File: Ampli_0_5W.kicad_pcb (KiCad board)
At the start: 2 copper layers, 100 x 81 mm, 70 parts, among them J1002 RF_In, J1003 PTT_In, J1005 Aux_PTT_Out, J1006 RF_Out, Q1001 2N7002, Q1002 FDD6685, Q1005 2N5109, Q1006 AFT05MP075N, T1001 4:1, T1002 1:1, T1003 1:9, U1001 L78L05_SO8

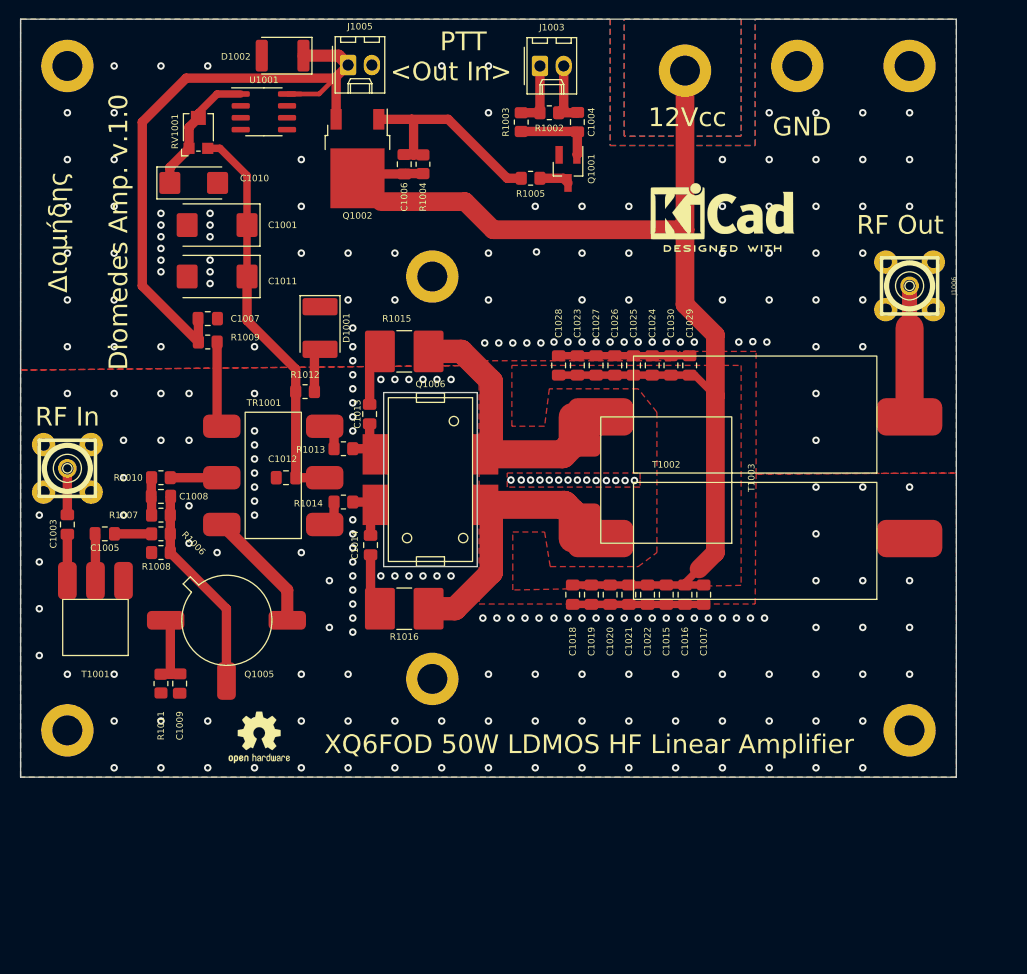
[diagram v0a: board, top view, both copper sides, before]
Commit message: release 2.0, shorter drain path
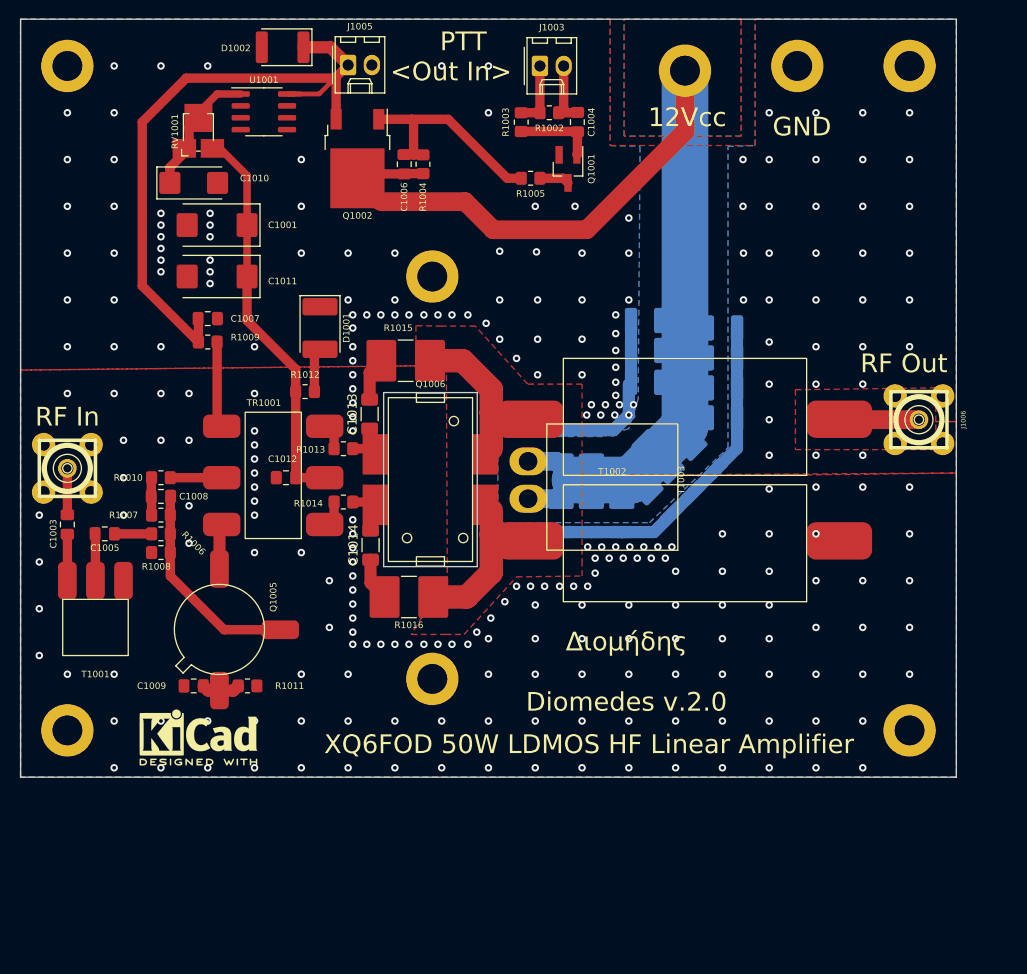
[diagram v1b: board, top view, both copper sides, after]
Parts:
- removed the REF** at (155.0, 50.5)
- removed the REF** at (105.5, 106.8)
- added REF**: KiCad-Logo2_5mm_SilkScreen, Symbol:KiCad-Logo2_5mm_SilkScreen, F.Cu at (99.0, 106.8)
- C1013, C1014: footprint Capacitor_SMD:C_0805_2012Metric_Pad1.18x1.45mm_HandSolder -> Capacitor_SMD:C_1206_3216Metric_Pad1.33x1.80mm_HandSolder
- C1015, C1016, C1017, C1018, C1019, C1020, C1021, C1022, C1023, C1024, C1025, C1026, C1027, C1028, C1029, C1030: footprint Capacitor_SMD:C_0805_2012Metric_Pad1.18x1.45mm_HandSolder -> Capacitor_SMD:C_1210_3225Metric_Pad1.33x2.70mm_HandSolder; moved to B.Cu
- moved C1017 22.2 mm to (155.0, 69.4), turned to 180 degrees
- moved C1016 19.3 mm to (155.0, 72.6), turned to 180 degrees
- moved C1015 15.1 mm to (153.2, 77.0), turned to 135 degrees
- moved J1006 14.3 mm to (176.0, 72.8)
- moved C1029 13.5 mm to (141.0, 75.5)
- moved C1022 12.6 mm to (150.8, 79.5), turned to 135 degrees
- moved C1021 10.4 mm to (148.5, 81.8), turned to 135 degrees
- moved R1011 9.25 mm to (104.2, 101.2), turned to 180 degrees
- moved C1023 9.22 mm to (145.5, 74.0), turned to -45 degrees
- moved C1028 8.50 mm to (137.8, 75.5)
- moved C1024 8.50 mm to (155.0, 63.0), turned to 180 degrees
- moved C1018 8.34 mm to (137.8, 83.2)
- moved C1020 8.34 mm to (144.2, 83.2)
- moved C1019 8.25 mm to (141.0, 83.2)
- moved T1003 7.50 mm to (151.5, 79.2)
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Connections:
- T1002 pad 1: Net-(Q1006-Pad3) -> decoupling
- T1002 pad 3: Net-(Q1006-Pad4) -> decoupling
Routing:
- net GND: track 35.2 -> 59.9 mm, vias 243 -> 269
- net decoupling: track 136.4 -> 122.3 mm
- net Net-(Q1006-Pad4): track 27.8 -> 18.7 mm
- net Net-(Q1006-Pad3): track 27.2 -> 18.4 mm
- net Net-(Q1005-Pad3): track 13.1 -> 4.85 mm
- net Net-(J1006-Pad1): track 14.0 -> 8.52 mm
- net Net-(C1009-Pad2): track 7.99 -> 4.13 mm
- net Net-(C1014-Pad2): track 5.99 -> 3.23 mm
- net Net-(C1013-Pad1): track 5.31 -> 2.65 mm
- net Net-(C1014-Pad1): track 6.18 -> 4.61 mm
- net Net-(C1013-Pad2): track 6.12 -> 4.66 mm
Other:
- board text added: "Διομήδης Diomedes v.2.0"
- board text removed: "Διομήδης Diomedes Amp. v.1.0"

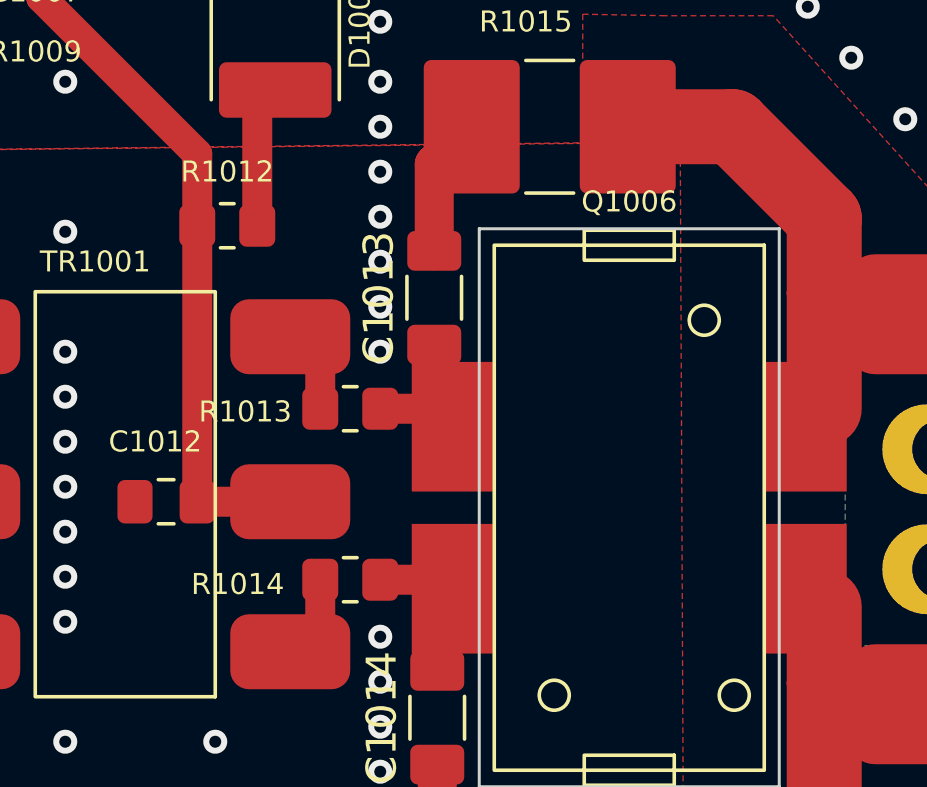
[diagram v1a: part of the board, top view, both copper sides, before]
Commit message: shorten drain circuit, new gerber, new ibom
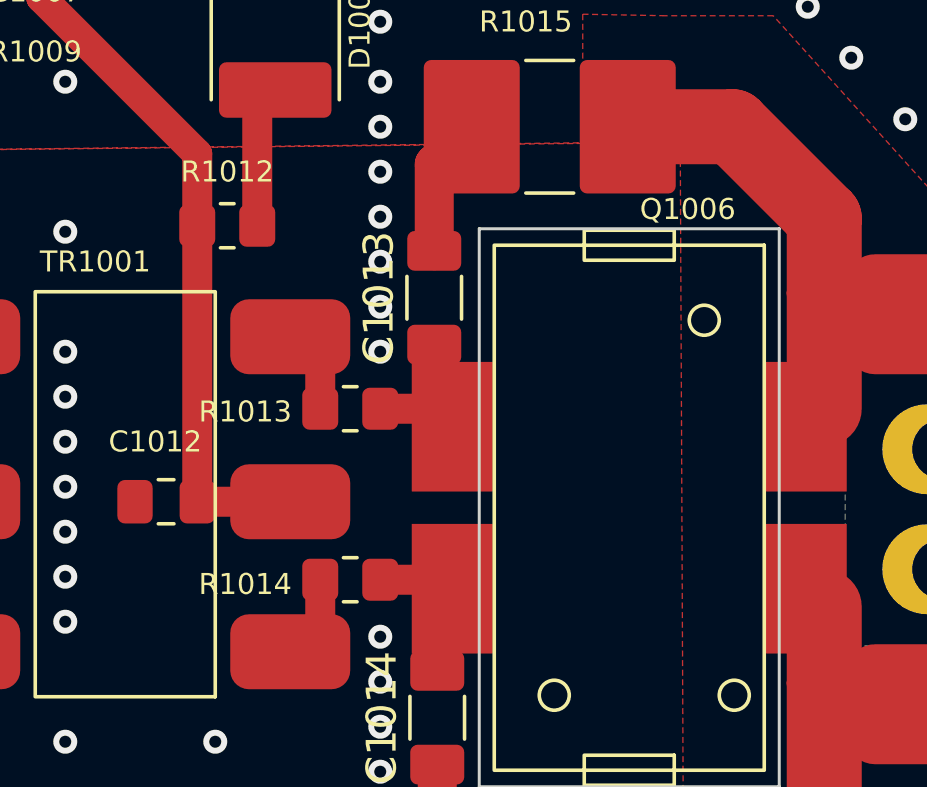
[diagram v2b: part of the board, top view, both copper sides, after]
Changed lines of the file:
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@@
     (property "Sheetname" "")
     (attr smd)
-    (fp_text reference "Q1006" (at 0 10.95 unlocked) (layer "F.SilkS")
+    (fp_text reference "Q1006" (at -1.95 10.7 unlocked) (layer "F.SilkS")
       (effects (font (size 0.7 0.7) (thickness 0.175)))
     )
@@
     (property "Sheetname" "")
     (attr smd)
-    (fp_text reference "R1014" (at 3.75 -0.15) (layer "F.SilkS")
+    (fp_text reference "R1014" (at 3.5 -0.15) (layer "F.SilkS")
       (effects (font (size 0.7 0.7) (thickness 0.15)))
     )
@@
     (effects (font (size 2 2) (thickness 0.4)))
   )
+  (dimension (type aligned) (layer "F.SilkS")
+    (pts (xy 131 80.25) (xy 90.5 80.5))
+    (height -61.983387)
+    (gr_text "40.5008 mm" (at 111.125507 141.207228 0.3536731592) (layer "F.SilkS")
+      (effects (font (size 1 1) (thickness 0.15)))
+    )
+    (format (units 3) (units_format 1) (precision 4))
+    (style (thickness 0.15) (arrow_length 1.27) (text_position_mode 0) (extension_height 0.58642) (extension_offset 0.5) keep_text_aligned)
+  )
+  (dimension (type aligned) (layer "F.SilkS")
+    (pts (xy 109.75 111) (xy 109 41))
+    (height 90.513554)
+    (gr_text "70.0040 mm" (at 201.033293 75.017947 -89.38614014) (layer "F.SilkS")
+      (effects (font (size 1 1) (thickness 0.15)))
+    )
+    (format (units 3) (units_format 1) (precision 4))
+    (style (thickness 0.15) (arrow_length 1.27) (text_position_mode 0) (extension_height 0.58642) (extension_offset 0.5) keep_text_aligned)
+  )
   (dimension (type aligned) (layer "Eco2.User")

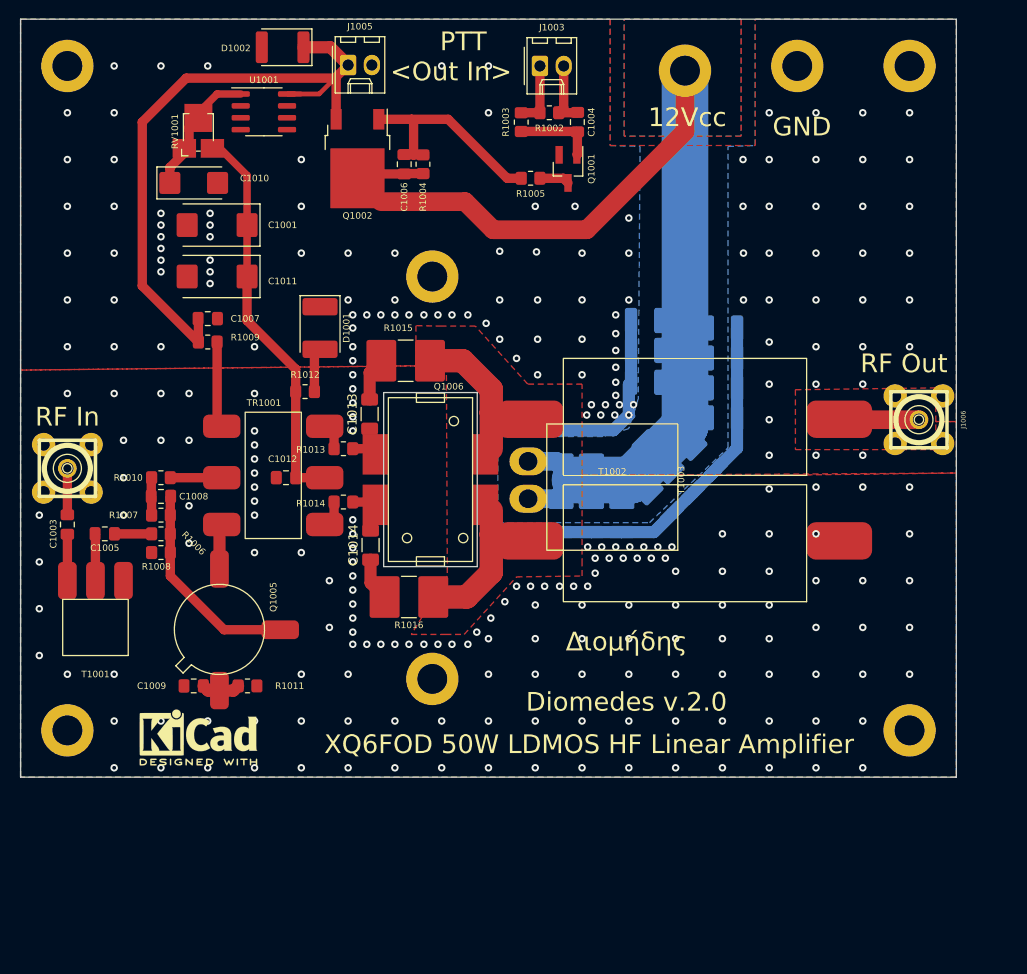
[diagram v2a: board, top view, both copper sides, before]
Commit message: Diomedes V1.0 final with correct psu, bias & drain trace
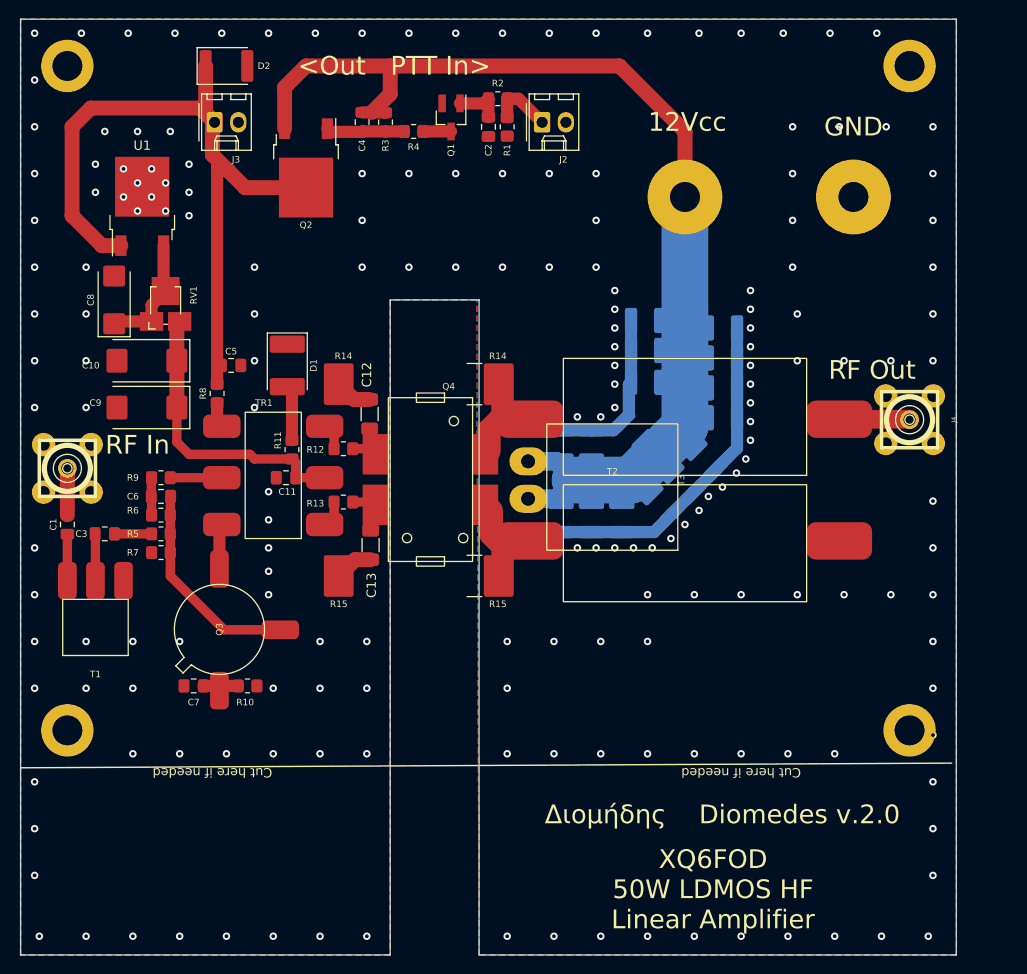
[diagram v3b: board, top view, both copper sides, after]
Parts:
- removed H1001, H1003: MountingHole_Pad, MountingHole:MountingHole_3.2mm_M3_DIN965_Pad
- removed REF**: KiCad-Logo2_5mm_SilkScreen, Symbol:KiCad-Logo2_5mm_SilkScreen
- U1: renamed from U1001; value L78L05_SO8 -> LM78M05_TO252; footprint Package_SO:SOIC-8_3.9x4.9mm_P1.27mm -> Package_TO_SOT_SMD:TO-252-2
- moved RV1 18.8 mm to (95.5, 60.5)
- moved U1 16.5 mm to (93.0, 50.0), turned to 90 degrees
- moved C10 16.3 mm to (93.5, 66.5)
- moved C9 15.9 mm to (93.5, 71.5)
- moved J3 15.5 mm to (100.7, 41.0)
- moved H2 15.2 mm to (169.0, 49.0)
- moved C8 15.1 mm to (90.0, 60.0), turned to 90 degrees
- moved Q1 13.7 mm to (126.0, 40.5)
- moved H1 13.5 mm to (151.0, 49.0)
- moved R4 13.5 mm to (122.0, 42.0)
- moved C2 9.51 mm to (130.0, 41.5), turned to -90 degrees
- moved R14 7.76 mm to (128.5, 69.0)
- moved R15 7.35 mm to (128.5, 89.5)
- moved C4 6.36 mm to (116.5, 41.0), turned to -90 degrees
- moved R11 6.36 mm to (109.0, 76.0), turned to -90 degrees
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- renumbered C1003 to C1, C1001 to C10, C1012 to C11, C1013 to C12, C1014 to C13, C1015 to C14, C1016 to C15, C1017 to C16, C1018 to C17, C1019 to C18, C1020 to C19, C1004 to C2, C1021 to C20, C1022 to C21, C1024 to C22, C1025 to C23, C1026 to C24, C1027 to C25, C1023 to C26, C1028 to C27, C1029 to C28, C1030 to C29, C1005 to C3, C1006 to C4, C1007 to C5, C1008 to C6, C1009 to C7, C1010 to C8, C1011 to C9, D1001 to D1, D1002 to D2, H1006 to H1, H1004 to H2, H1002 to H4, H1005 to H6, H1007 to H7, H1008 to H8, J1002 to J1, J1003 to J2, J1005 to J3, J1006 to J4, Q1001 to Q1, Q1002 to Q2, Q1005 to Q3, Q1006 to Q4, R1002 to R1, R1011 to R10, R1012 to R11, R1013 to R12, R1014 to R13, R1015 to R14, R1016 to R15, R1003 to R2, R1004 to R3, R1005 to R4, R1006 to R5, R1007 to R6, R1008 to R7, R1009 to R8, R1010 to R9, RV1001 to RV1, T1001 to T1, T1002 to T2, T1003 to T3, TR1001 to TR1
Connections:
- C5 pad 1: Net-(C1007-Pad1) -> Net-(C5-Pad1)
- C8 pad 1: Net-(C1010-Pad1) -> Net-(C8-Pad1)
- D2 pad 1: Net-(C1007-Pad1) -> Net-(C5-Pad1)
- J3 pad 1: Net-(C1007-Pad1) -> Net-(C5-Pad1)
- Q2 pad 2: decoupling -> Net-(C5-Pad1)
- Q2 pad 3: Net-(C1007-Pad1) -> decoupling
- Q4 pad 3: Net-(Q1006-Pad3) -> Net-(Q4-Pad3)
- Q4 pad 4: Net-(Q1006-Pad4) -> Net-(Q4-Pad3)
- R14 pad 1: Net-(Q1006-Pad4) -> Net-(Q4-Pad3)
- R15 pad 1: Net-(Q1006-Pad3) -> Net-(Q4-Pad3)
- R8 pad 2: Net-(C1007-Pad1) -> Net-(C5-Pad1)
- RV1 pad 1: Net-(C1010-Pad1) -> Net-(C8-Pad1)
- RV1 pad 2: Net-(C1010-Pad1) -> Net-(C8-Pad1)
- T3 pad 1: Net-(Q1006-Pad4) -> Net-(Q4-Pad3)
- T3 pad 2: Net-(Q1006-Pad3) -> Net-(Q4-Pad3)
- U1 pad 1: Net-(C1010-Pad1) -> Net-(C5-Pad1)
- U1 pad 3: GND -> Net-(C8-Pad1)
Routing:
- net Net-(C5-Pad1): track 0.00 -> 78.9 mm
- net Net-(C1007-Pad1): track 72.9 -> 0.00 mm
- net Net-(Q4-Pad3): track 0.00 -> 24.4 mm
- net Net-(Q1006-Pad4): track 18.7 -> 0.00 mm
- net Net-(Q1006-Pad3): track 18.4 -> 0.00 mm
- net Net-(C4-Pad2): track 23.7 -> 8.38 mm
- net Net-(C1010-Pad1): track 14.1 -> 0.00 mm
- net Net-(C8-Pad1): track 0.00 -> 12.9 mm
- net Net-(C10-Pad1): track 43.0 -> 31.3 mm
- net GND: track 59.9 -> 52.7 mm, vias 269 -> 185
- net Net-(R8-Pad1): track 9.21 -> 2.00 mm
- net decoupling: track 122.3 -> 117.7 mm
- net Net-(C2-Pad1): track 8.50 -> 5.22 mm
- net Net-(D1-Pad2): track 4.77 -> 5.93 mm
- net Net-(J4-Pad1): track 8.52 -> 7.59 mm
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- removed copper zone on B.Cu, net decoupling
- removed copper zone on F.Cu, net decoupling
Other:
- board size 100 x 81 mm -> 100 x 100 mm
- board text added: "<Out PTT In>"
- board text added: "Cut here if needed"
- board text added: "R14"
- board text added: "R15"
- board text removed: "PTT <Out In>"

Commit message: Diomedes V2.0 final, bias OK
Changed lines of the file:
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@@
     (effects (font (size 0.7 0.7) (thickness 0.15)))
-  )
-  (gr_text "Διομήδης    Diomedes v.2.0\n" (at 155 115) (layer "F.SilkS")
-    (effects (font (size 2 2) (thickness 0.4)))
   )
   (gr_text "Cut here if needed" (at 157 110.5 180) (layer "F.SilkS")
     (effects (font (size 1 1) (thickness 0.15)))
   )
+  (gr_text "Διομήδης    Diomedes v.2.0\n" (at 153 99) (layer "F.SilkS")
+    (effects (font (size 2 2) (thickness 0.4)))
+  )
   (gr_text "GND" (at 169 41.5) (layer "F.SilkS")

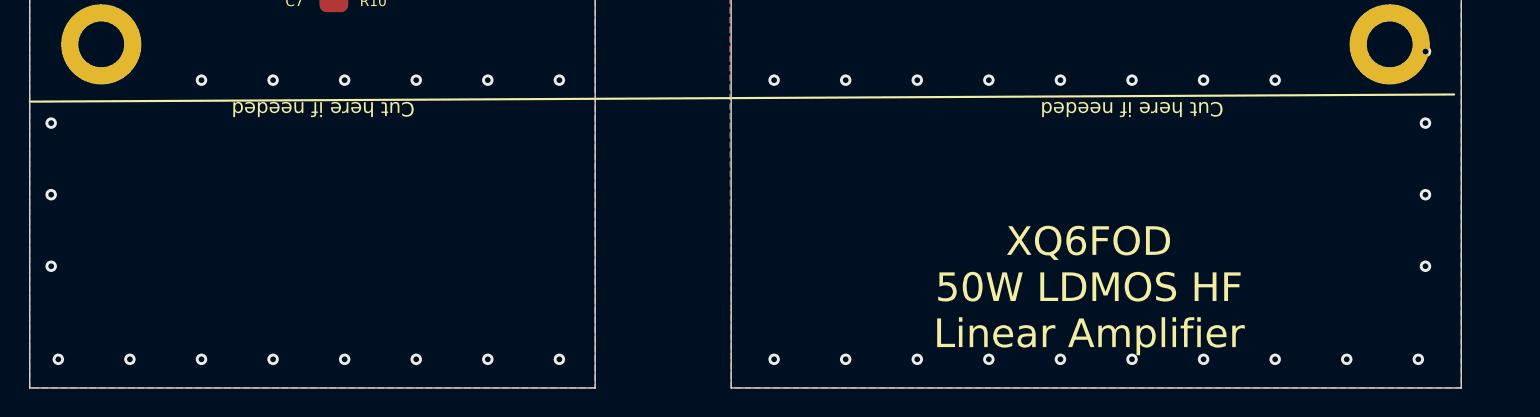
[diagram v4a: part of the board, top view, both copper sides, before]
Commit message: new ibom, BEWARE, KICAD 7.0 FILE FORMAT
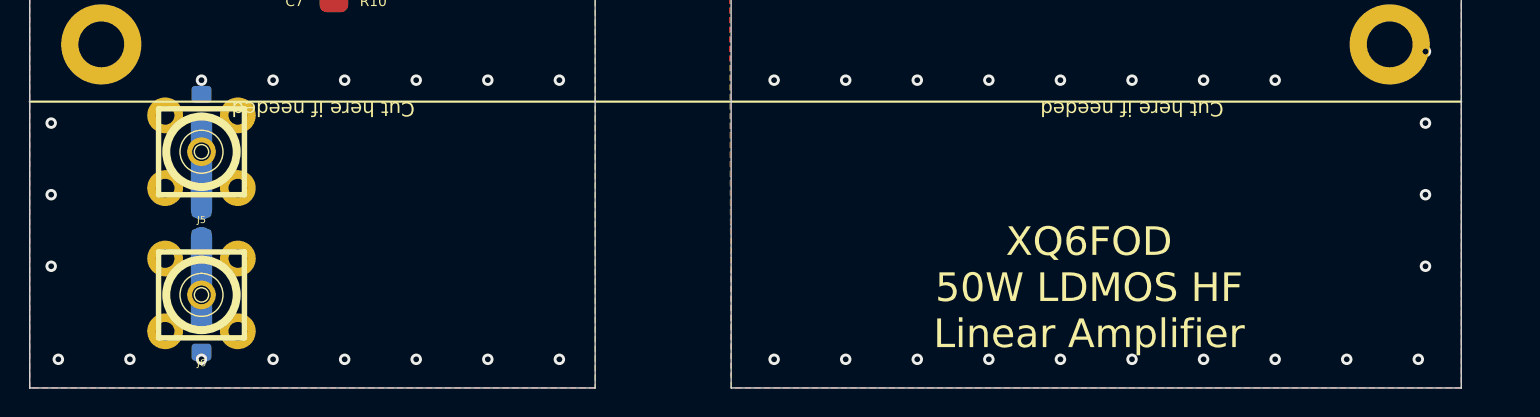
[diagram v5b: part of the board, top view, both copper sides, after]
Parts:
- added J5: RF_Out, SMA_PINS:SMA_PINS, F.Cu at (92.0, 113.5)
- added J6: RF_Out, SMA_PINS:SMA_PINS, F.Cu at (92.0, 123.5)
- added R16: 62R, Resistor_SMD:R_0805_2012Metric_Pad1.20x1.40mm_HandSolder, B.Cu at (92.0, 110.5)
- added R17: 249R, Resistor_SMD:R_0805_2012Metric_Pad1.20x1.40mm_HandSolder, B.Cu at (92.0, 118.5)
- added R18: 62R, Resistor_SMD:R_0805_2012Metric_Pad1.20x1.40mm_HandSolder, B.Cu at (92.0, 126.5)
- R5: value 6.8R -> 8.2R
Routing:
- net Net-(J6-Pad1): track 0.00 -> 6.00 mm
- net Net-(J5-Pad1): track 0.00 -> 6.00 mm
